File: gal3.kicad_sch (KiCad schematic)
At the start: 9 parts, among them IC13 SN74ALS374N, IC8 SN74ALS374N, IC9 D65200GD076

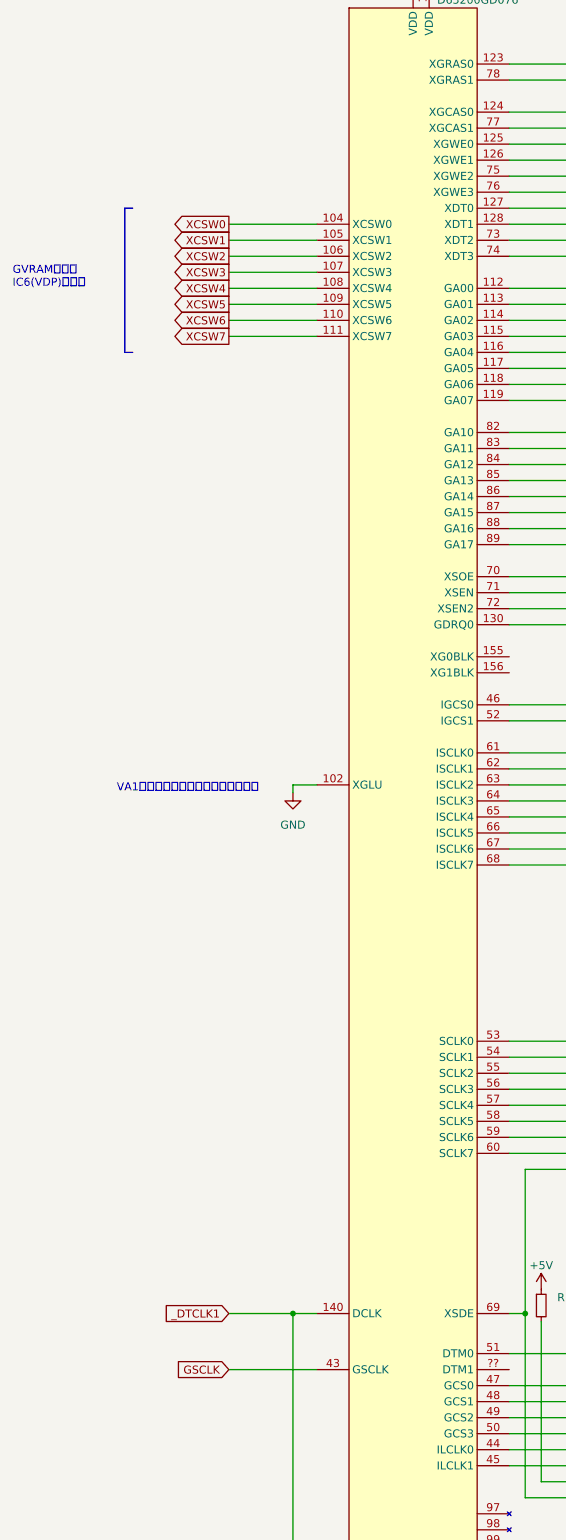
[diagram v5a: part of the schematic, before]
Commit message: schematic: wire IC1 and CN4
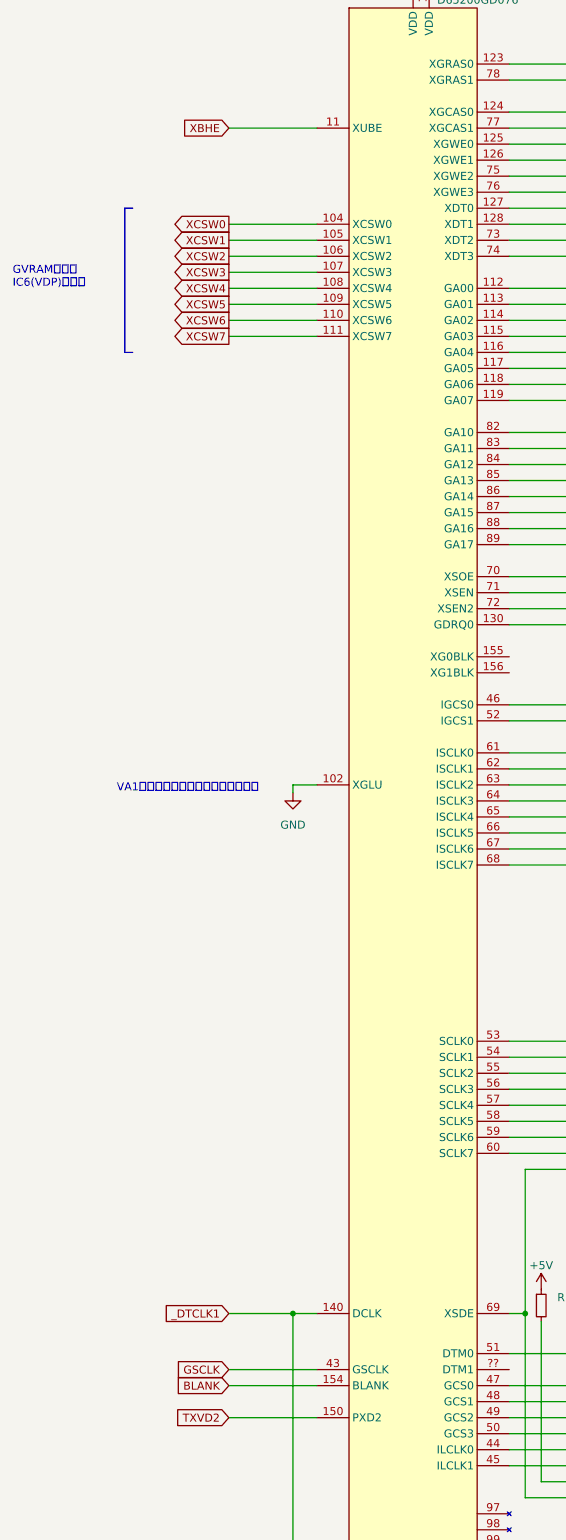
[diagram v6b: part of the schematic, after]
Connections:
- new net BLANK: IC9.154 (BLANK)
- new net TXVD2: IC9.150 (PXD2)
- new net XBHE: IC9.11 (XUBE)
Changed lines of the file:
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@@
+    (stroke (width 0) (type default))
+  )
+  (wire (pts (xy 59.69 259.08) (xy 73.66 259.08))
     (stroke (width 0) (type default))
   )
@@
     (stroke (width 0) (type default))
   )
+  (wire (pts (xy 59.69 264.16) (xy 73.66 264.16))
+    (stroke (width 0) (type default))
+  )
   (wire (pts (xy 191.77 254) (xy 191.77 266.7))
     (stroke (width 0) (type default))
@@
   )
   (wire (pts (xy 189.23 212.09) (xy 204.47 212.09))
+    (stroke (width 0) (type default))
+  )
+  (wire (pts (xy 59.69 59.69) (xy 73.66 59.69))
     (stroke (width 0) (type default))
   )
@@
     )
   )
+  (global_label "XBHE" (shape input) (at 59.69 59.69 180) (fields_autoplaced)
+    (effects (font (size 1.27 1.27)) (justify right))
+    (property "Intersheetrefs" "${INTERSHEET_REFS}" (at 51.7458 59.69 0)
+      (effects (font (size 1.27 1.27)) (justify right) hide)
+    )
+  )
+  (global_label "BLANK" (shape input) (at 59.69 259.08 180) (fields_autoplaced)
+    (effects (font (size 1.27 1.27)) (justify right))
+    (property "Intersheetrefs" "${INTERSHEET_REFS}" (at 50.7176 259.08 0)
+      (effects (font (size 1.27 1.27)) (justify right) hide)
+    )
+  )
   (global_label "GA01" (shape output) (at 125.73 87.63 0) (fields_autoplaced)
     (effects (font (size 1.27 1.27)) (justify left))
@@
     (property "Intersheetrefs" "${INTERSHEET_REFS}" (at 135.8513 77.47 0)
       (effects (font (size 1.27 1.27)) (justify left) hide)
+    )
+  )
+  (global_label "TXVD2" (shape input) (at 59.69 264.16 180) (fields_autoplaced)
+    (effects (font (size 1.27 1.27)) (justify right))
+    (property "Intersheetrefs" "${INTERSHEET_REFS}" (at 50.9596 264.16 0)
+      (effects (font (size 1.27 1.27)) (justify right) hide)
     )
   )
@@
     (pin "101")
     (pin "100")
+    (pin "150")
+    (pin "154")
+    (pin "11")
     (instances
       (project "88va2-circuit"

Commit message: schematic: tidy hierarchical sheets
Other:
- title: (none) -> GAL-3
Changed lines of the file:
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@@
   (paper "A3" portrait)
   (title_block
+    (title "GAL-3")
     (comment 1 "VA1回路図 P.253")
   )
